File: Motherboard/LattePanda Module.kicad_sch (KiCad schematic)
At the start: 89 parts, among them IC78 PCM2704CDBR, J3 Conn_01x03_Pin, J5 SM03B-SRSS-TB, J78 Speaker_L, J79 Speaker_R, SW78 SW_Push, SW79 SW_Push, SW80 SW_Push, SW81 SW_Push, U10 ULC0524P, U11 ULC0524P, U12 ULC0524P, U78 RP2040, U84 PAM8403D, U88 RP2354B, U95 W25Q128JVS, Y1 ABM8-272-T3, Y2 ABM8-272-T3, Y78 Crystal

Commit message: Multiplexed Debug HDMI port with DDIB screen, there are no BIOS versions with HDMI out on TCP1.
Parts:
- added IC79: TS3DV621RUAR, QFN50P350X900X80-43N-D, symbol TS3DV621RUAR:TS3DV621RUAR
- added SW82: SW_Nidec_CAS-120A1, Button_Switch_SMD:Nidec_Copal_CAS-120A, symbol Switch:SW_Nidec_CAS-120A1
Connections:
- net +3V3: now also IC79.1 (VCC_1), IC79.17 (VCC_2), IC79.30 (VCC_3), IC79.8 (EN), SW82.3 (A)
- net DBUG_HPD: now also IC79.20 (HPDB); no longer A2.185 (TCP1_HPD)
- net DBUG_SCL: now also IC79.22 (AUX-B); no longer A2.175 (TCP1_DDC_SCL)
- net DBUG_SDA: now also IC79.24 (AUX+B); no longer A2.173 (TCP1_DDC_SDA)
- net DBUG_TX0+: now also IC79.42 (D0+B); no longer A2.220 (TCP1_TX0+)
- net DBUG_TX0-: now also IC79.40 (D0-B); no longer A2.222 (TCP1_TX0-)
- net DBUG_TX1+: now also IC79.37 (D1+B); no longer A2.226 (TCP1_TXRX0+)
- net DBUG_TX1-: now also IC79.35 (D1-B); no longer A2.228 (TCP1_TXRX0-)
- net DBUG_TX2+: now also IC79.33 (D2+B); no longer A2.232 (TCP1_TX1+)
- net DBUG_TX2-: now also IC79.31 (D2-B); no longer A2.234 (TCP1_TX1-)
- net DBUG_TX3+: now also IC79.28 (D3+B); no longer A2.238 (TCP1_TXRX1+)
- net DBUG_TX3-: now also IC79.26 (D3-B); no longer A2.240 (TCP1_TXRX1-)
- net DDIB_HPD: now also IC79.21 (HPDA); no longer A2.183 (DDIB_HPD)
- net DDIB_SCL: now also IC79.23 (AUX-A); no longer A2.171 (DDIB_DDC_SCL)
- net DDIB_SDA: now also IC79.25 (AUX+A); no longer A2.169 (DDIB_DDC_SDA)
- net DDIB_TX0+: now also IC79.41 (D0+A); no longer A2.217 (DDIB_TX0+)
- net DDIB_TX0-: now also IC79.39 (D0-A); no longer A2.215 (DDIB_TX0-)
- net DDIB_TX1+: now also IC79.38 (D1+A); no longer A2.211 (DDIB_TX1+)
- net DDIB_TX1-: now also IC79.36 (D1-A); no longer A2.209 (DDIB_TX1-)
- net DDIB_TX2+: now also IC79.34 (D2+A); no longer A2.205 (DDIB_TX2+)
- net DDIB_TX2-: now also IC79.32 (D2-A); no longer A2.203 (DDIB_TX2-)
- net DDIB_TX3+: now also IC79.29 (D3+A); no longer A2.199 (DDIB_TX3+)
- net DDIB_TX3-: now also IC79.27 (D3-A); no longer A2.197 (DDIB_TX3-)
- net GND: now also IC79.43 (EP_(GND)), SW82.1 (C)
- net SLS_S3: now also U88.42 (GPIO33)
- net ~{PWR_LED}/~{PSON}: now also U88.40 (GPIO32)
- new net: IC79.10 (SEL2), IC79.9 (SEL1), SW82.2 (B)
- new net DDI_HPD: A2.183 (DDIB_HPD), IC79.15 (HPD)
- new net DDI_SCL: A2.171 (DDIB_DDC_SCL), IC79.14 (AUX-)
- new net DDI_SDA: A2.169 (DDIB_DDC_SDA), IC79.13 (AUX+)
- new net DDI_TX0+: A2.217 (DDIB_TX0+), IC79.2 (D0+)
- new net DDI_TX0-: A2.215 (DDIB_TX0-), IC79.3 (D0-)
- new net DDI_TX1+: A2.211 (DDIB_TX1+), IC79.4 (D1+)
- new net DDI_TX1-: A2.209 (DDIB_TX1-), IC79.5 (D1-)
- new net DDI_TX2+: A2.205 (DDIB_TX2+), IC79.6 (D2+)
- new net DDI_TX2-: A2.203 (DDIB_TX2-), IC79.7 (D2-)
- new net DDI_TX3+: A2.199 (DDIB_TX3+), IC79.11 (D3+)
- new net DDI_TX3-: A2.197 (DDIB_TX3-), IC79.12 (D3-)
- no-connect marks 120 -> 131
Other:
- note removed: "(They are all used because I need an extra one to configure the ADV7611. Because we CANT have defaults, we MUST use I2C)"

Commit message: Quick Save
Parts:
- A2: LCSC Part C2761395 -> C962120; NOTE (none) -> LOTES ADDR0207-P001A connector
- H10, H9: LCSC Part C5301799 -> C2928178
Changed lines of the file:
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@@
 			)
 		)
-		(property "Sim.Device" ""
+		(property "NOTE" "LOTES ADDR0207-P001A connector"
 			(at 311.15 190.5 0)
 			(hide yes)
@@
 			)
 		)
-		(property "LCSC Part" "C2761395"
+		(property "LCSC Part" "C962120"
 			(at 311.15 190.5 0)
 			(hide yes)
@@
 			)
 		)
-		(property "Description" "SMTWEM250STR"
+		(property "Description" "SMTWE2025MTJ"
 			(at 297.18 345.44 0)
 			(hide yes)
@@
 			)
 		)
-		(property "LCSC Part" "C5301799"
+		(property "LCSC Part" "C2928178"
 			(at 297.18 345.44 0)
 			(hide yes)
@@
 			)
 		)
-		(property "Description" "SMTWEM250STR"
+		(property "Description" "SMTWE2025MTJ"
 			(at 322.58 345.44 0)
 			(hide yes)
@@
 			)
 		)
-		(property "LCSC Part" "C5301799"
+		(property "LCSC Part" "C2928178"
 			(at 322.58 345.44 0)
 			(hide yes)

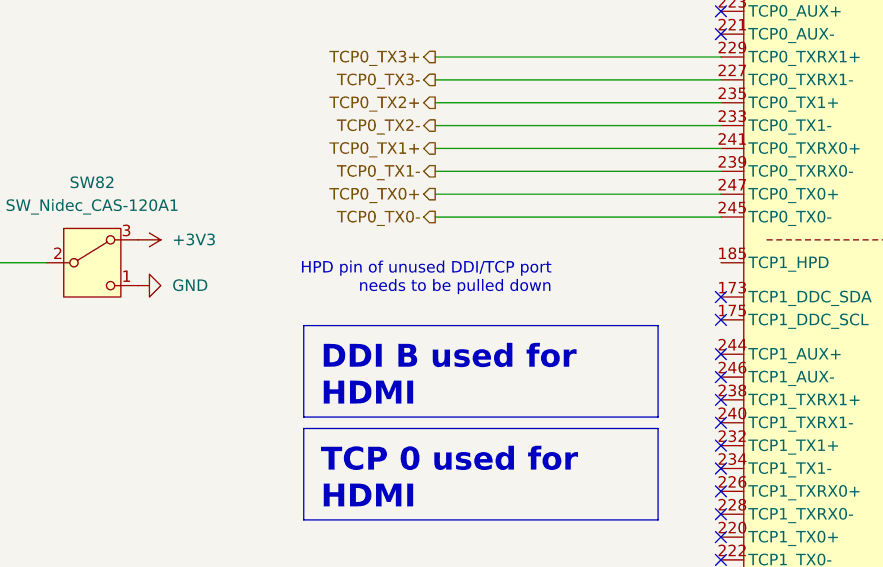
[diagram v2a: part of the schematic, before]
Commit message: Re-Routed DDIB Screen, pinout was previously flipped
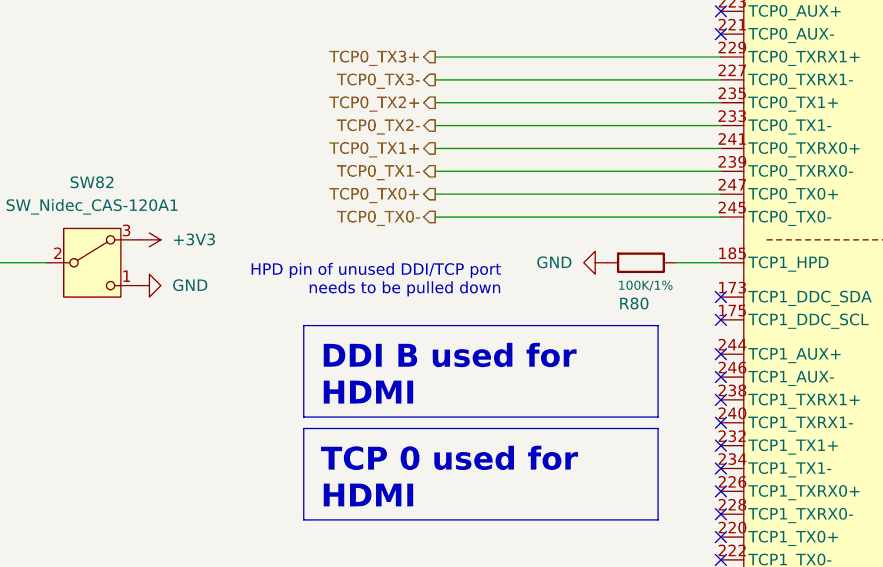
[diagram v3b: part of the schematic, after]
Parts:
- added R80: 100K/1%, A_HDJ_Library:R_0402_1005Metric, symbol Device:R
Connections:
- net GND: now also R80.2
- net at A2.185 (TCP1_HPD): now also R80.1

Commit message: Various fixes, and some peripheral routing
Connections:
- net Col3: no longer U88.79 (GPIO2)
- net Col4: no longer U88.80 (GPIO3)
- net RPi_HALL_L: now also U88.80 (GPIO3); no longer U88.20 (GPIO20)
- net RPi_LCD_EN: now also U88.79 (GPIO2); no longer U88.22 (GPIO22)
- net Row1: now also U88.2 (GPIO5); no longer U88.1 (GPIO4)
- net Row2: now also U88.3 (GPIO6); no longer U88.2 (GPIO5)
- net Row3: now also U88.1 (GPIO4); no longer U88.3 (GPIO6)
- no-connect marks 131 -> 132
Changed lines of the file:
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@@
 	)
 	(no_connect
+		(at 270.51 165.1)
+	)
+	(no_connect
 		(at 351.79 87.63)
 	)
@@
 		)
 	)
-	(hierarchical_label "Col3"
-		(shape output)
-		(at 510.54 130.81 0)
-		(effects
-			(font
-				(size 1.27 1.27)
-			)
-			(justify left)
-		)
-	)
 	(hierarchical_label "~{PWR_SW}"
 		(shape input)
@@
 		)
 	)
+	(hierarchical_label "Col4"
+		(shape output)
+		(at 541.02 133.35 0)
+		(effects
+			(font
+				(size 1.27 1.27)
+			)
+			(justify left)
+		)
+	)
 	(hierarchical_label "HSIO_3_TX+"
 		(shape output)
@@
 	(hierarchical_label "Row3"
 		(shape input)
-		(at 510.54 140.97 0)
+		(at 510.54 135.89 0)
 		(effects
 			(font
@@
 	(hierarchical_label "DDIB_TOUCH_SCL"
 		(shape input)
-		(at 351.79 220.98 0)
+		(at 351.79 220.98 180)
 		(effects
 			(font
 				(size 1.27 1.27)
 			)
-			(justify left)
+			(justify right)
 		)
 	)
 	(hierarchical_label "Row1"
 		(shape input)
-		(at 510.54 135.89 0)
+		(at 510.54 138.43 0)
 		(effects
 			(font
@@
 	(hierarchical_label "RPi_HALL_L"
 		(shape output)
-		(at 510.54 176.53 0)
+		(at 510.54 133.35 0)
 		(effects
 			(font
@@
 		)
 	)
-	(hierarchical_label "RPi_LCD_EN"
-		(shape passive)
-		(at 510.54 181.61 0)
-		(effects
-			(font
-				(size 1.27 1.27)
-			)
-			(justify left)
-		)
-	)
 	(hierarchical_label "TCP0_TX3-"
 		(shape output)
@@
 		)
 	)
+	(hierarchical_label "Col3"
+		(shape output)
+		(at 541.02 130.81 0)
+		(effects
+			(font
+				(size 1.27 1.27)
+			)
+			(justify left)
+		)
+	)
 	(hierarchical_label "TCP0_TX3+"
 		(shape output)
@@
 		)
 	)
-	(hierarchical_label "Col4"
-		(shape output)
-		(at 510.54 133.35 0)
-		(effects
-			(font
-				(size 1.27 1.27)
-			)
-			(justify left)
-		)
-	)
 	(hierarchical_label "DDIB_TOUCH_SDA"
 		(shape bidirectional)
@@
 		)
 	)
+	(hierarchical_label "RPi_LCD_EN"
+		(shape passive)
+		(at 510.54 130.81 0)
+		(effects
+			(font
+				(size 1.27 1.27)
+			)
+			(justify left)
+		)
+	)
 	(hierarchical_label "L_ADC_X"
 		(shape output)
@@
 	(hierarchical_label "TCP0_TOUCH_SCL"
 		(shape input)
-		(at 351.79 218.44 0)
+		(at 351.79 218.44 180)
 		(effects
 			(font
 				(size 1.27 1.27)
 			)
-			(justify left)
+			(justify right)
 		)
 	)
 	(hierarchical_label "Row2"
 		(shape input)
-		(at 510.54 138.43 0)
+		(at 510.54 140.97 0)
 		(effects
 			(font

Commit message: Updated CTRLs to be one sided (saves a billion dollars somehow), added LCSC_Parts for BOM, and other fixes. (Part 1/2)
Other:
- note added: "???"
- note added: "HSIO 2"
- note added: "HSIO 3"
- note added: "HSIO 6"
- note added: "HSIO 8"
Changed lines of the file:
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@@
+		)
+	)
+	(text "HSIO 3\n\n\n"
+		(exclude_from_sim no)
+		(at 335.026 101.092 0)
+		(effects
+			(font
+				(size 1.27 1.27)
+			)
 		)
 	)
@@
 		)
 	)
+	(text "HSIO 8\n\n"
+		(exclude_from_sim no)
+		(at 335.026 95.25 0)
+		(effects
+			(font
+				(size 1.27 1.27)
+			)
+		)
+	)
 	(text "Sleeping State Signal\n\n- SLS_S0: \n  - S0 (Working): HIGH\n  - S3 (Slpeeping): LOW\n  - S4 (Hibernation): LOW\n  - S5 (Soft Off): LOW\n- SLS_S3:\n  - S0 (Working): HIGH\n  - S3 (Slpeeping): HIGH\n  - S4 (Hibernation): LOW\n  - S5 (Soft Off): LOW"
 		(exclude_from_sim no)
@@
 		)
 	)
+	(text "HSIO 6\n\n\n\n"
+		(exclude_from_sim no)
+		(at 335.28 107.696 0)
+		(effects
+			(font
+				(size 1.27 1.27)
+			)
+		)
+	)
 	(text "USB2_P6 is reserved for TypeC PD Controller\nDO NOT use it as a normal USB"
 		(exclude_from_sim no)
@@
 			)
 			(justify left)
+		)
+	)
+	(text "???\n"
+		(exclude_from_sim no)
+		(at 336.804 89.154 0)
+		(effects
+			(font
+				(size 1.27 1.27)
+			)
 		)
 	)
@@
 		)
 	)
+	(text "HSIO 8\n\n\n\n"
+		(exclude_from_sim no)
+		(at 263.652 129.286 0)
+		(effects
+			(font
+				(size 1.27 1.27)
+			)
+		)
+	)
+	(text "HSIO 6\n\n\n\n"
+		(exclude_from_sim no)
+		(at 264.16 171.958 0)
+		(effects
+			(font
+				(size 1.27 1.27)
+			)
+		)
+	)
 	(text "Have to send just 1 message on this I2C lane,\nbecause 5A charging isn't the default, 1A is. \nThis makes charging take 5hrs instead of 25.\nWHY... I HATE I2C."
 		(exclude_from_sim no)
@@
 		)
 	)
+	(text "HSIO 2\n"
+		(exclude_from_sim no)
+		(at 335.026 84.074 0)
+		(effects
+			(font
+				(size 1.27 1.27)
+			)
+		)
+	)

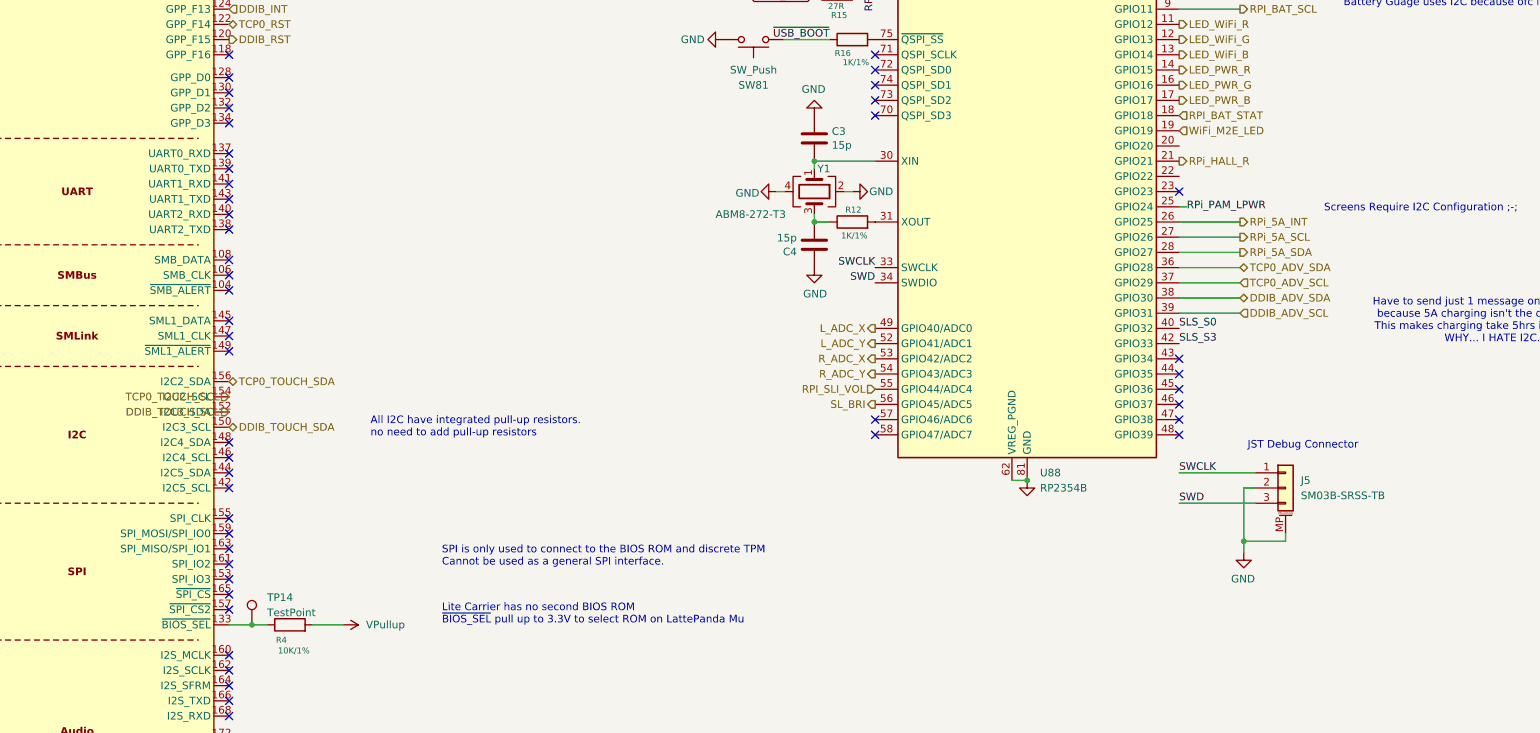
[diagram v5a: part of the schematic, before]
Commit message: Completed routing of 9V and 3.3V of PSU
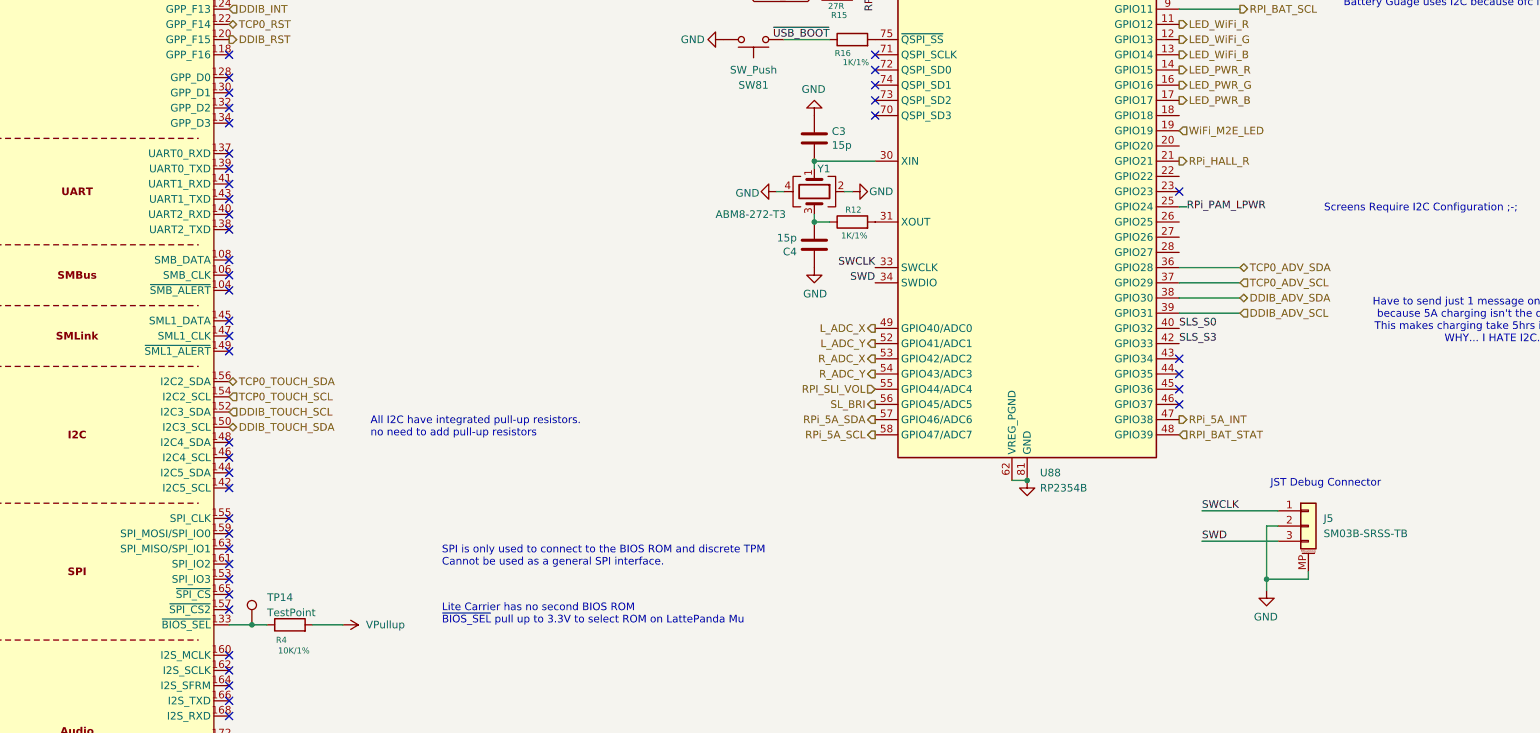
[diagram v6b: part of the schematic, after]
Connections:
- net RPI_BAT_STAT: now also U88.48 (GPIO39); no longer U88.18 (GPIO18)
- net RPi_5A_INT: now also U88.47 (GPIO38); no longer U88.26 (GPIO25)
- net RPi_5A_SCL: now also U88.58 (GPIO47/ADC7); no longer U88.27 (GPIO26)
- net RPi_5A_SDA: now also U88.57 (GPIO46/ADC6); no longer U88.28 (GPIO27)
- no-connect marks 132 -> 128
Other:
- moved on the sheet: J5
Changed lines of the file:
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@@
 	(text "JST Debug Connector"
 		(exclude_from_sim no)
-		(at 521.97 227.33 0)
+		(at 525.78 233.68 0)
 		(effects
 			(font
@@
 	)
 	(junction
-		(at 521.335 242.57)
+		(at 525.145 248.92)
 		(diameter 0)
 		(color 0 0 0 0)
@@
 	)
 	(no_connect
-		(at 459.74 222.25)
-	)
-	(no_connect
 		(at 270.51 299.72)
 	)
@@
 	)
 	(no_connect
-		(at 459.74 224.79)
-	)
-	(no_connect
 		(at 270.51 149.86)
 	)
@@
 	)
 	(no_connect
-		(at 510.54 224.79)
-	)
-	(no_connect
-		(at 510.54 222.25)
-	)
-	(no_connect
 		(at 270.51 157.48)
 	)
@@
 	(wire
 		(pts
-			(xy 521.335 233.68) (xy 521.335 242.57)
+			(xy 525.145 240.03) (xy 525.145 248.92)
 		)
 		(stroke
@@
 	(wire
 		(pts
-			(xy 510.54 231.14) (xy 523.24 231.14)
+			(xy 514.35 237.49) (xy 527.05 237.49)
 		)
 		(stroke
@@
 	(wire
 		(pts
-			(xy 528.32 241.3) (xy 528.32 242.57)
+			(xy 532.13 247.65) (xy 532.13 248.92)
 		)
 		(stroke
@@
 	(wire
 		(pts
-			(xy 510.54 236.22) (xy 523.24 236.22)
+			(xy 514.35 242.57) (xy 527.05 242.57)
 		)
 		(stroke
@@
 	(wire
 		(pts
-			(xy 520.7 189.23) (xy 510.54 189.23)
-		)
-		(stroke
-			(width 0)
-			(type default)
-		)
-	)
-	(wire
-		(pts
 			(xy 351.79 119.38) (xy 369.57 119.38)
 		)
@@
 	(wire
 		(pts
-			(xy 520.7 194.31) (xy 510.54 194.31)
-		)
-		(stroke
-			(width 0)
-			(type default)
-		)
-	)
-	(wire
-		(pts
 			(xy 459.74 328.93) (xy 459.74 334.01)
 		)
@@
 	(wire
 		(pts
-			(xy 521.335 242.57) (xy 528.32 242.57)
+			(xy 525.145 248.92) (xy 532.13 248.92)
 		)
 		(stroke
@@
 	(wire
 		(pts
-			(xy 521.335 242.57) (xy 521.335 244.475)
+			(xy 525.145 248.92) (xy 525.145 250.825)
 		)
 		(stroke
@@
 	(wire
 		(pts
-			(xy 520.7 191.77) (xy 510.54 191.77)
-		)
-		(stroke
-			(width 0)
-			(type default)
-		)
-	)
-	(wire
-		(pts
 			(xy 520.7 199.39) (xy 510.54 199.39)
 		)
@@
 	(wire
 		(pts
-			(xy 523.24 233.68) (xy 521.335 233.68)
+			(xy 527.05 240.03) (xy 525.145 240.03)
 		)
 		(stroke
@@
 	)
 	(label "SWD"
-		(at 510.54 236.22 0)
+		(at 514.35 242.57 0)
 		(effects
 			(font
@@
 	)
 	(label "SWCLK"
-		(at 510.54 231.14 0)
+		(at 514.35 237.49 0)
 		(effects
 			(font
@@
 		)
 	)
+	(hierarchical_label "RPi_5A_SCL"
+		(shape output)
+		(at 459.74 224.79 180)
+		(effects
+			(font
+				(size 1.27 1.27)
+			)
+			(justify right)
+		)
+	)
 	(hierarchical_label "LED_WiFi_B"
 		(shape output)
@@
 		)
 	)
-	(hierarchical_label "RPi_5A_SDA"
-		(shape output)
-		(at 520.7 194.31 0)
-		(effects
-			(font
-				(size 1.27 1.27)
-			)
-			(justify left)
-		)
-	)
 	(hierarchical_label "RPI_BAT_SDA"
 		(shape bidirectional)
@@
 		)
 	)
+	(hierarchical_label "RPi_5A_SDA"
+		(shape output)
+		(at 459.74 222.25 180)
+		(effects
+			(font
+				(size 1.27 1.27)
+			)
+			(justify right)
+		)
+	)
 	(hierarchical_label "DBUG_TX0-"
 		(shape output)
@@
 	(hierarchical_label "RPI_BAT_STAT"
 		(shape input)
-		(at 510.54 171.45 0)
+		(at 510.54 224.79 0)
 		(effects
 			(font
@@
 	(hierarchical_label "DDIB_TOUCH_SCL"
 		(shape input)
-		(at 351.79 220.98 180)
+		(at 351.79 220.98 0)
 		(effects
 			(font
 				(size 1.27 1.27)
 			)
-			(justify right)
+			(justify left)
 		)
 	)
@@
 		)
 	)
+	(hierarchical_label "RPi_5A_INT"
+		(shape output)
+		(at 510.54 222.25 0)
+		(effects
+			(font
+				(size 1.27 1.27)
+			)
+			(justify left)
+		)
+	)
 	(hierarchical_label "Col3"
 		(shape output)
@@
 		)
 	)
-	(hierarchical_label "RPi_5A_INT"
-		(shape output)
-		(at 520.7 189.23 0)
-		(effects
-			(font
-				(size 1.27 1.27)
-			)
-			(justify left)
-		)
-	)
 	(hierarchical_label "HSIO_2_TX-"
 		(shape output)
@@
 		)
 	)
-	(hierarchical_label "RPi_5A_SCL"
-		(shape output)
-		(at 520.7 191.77 0)
-		(effects
-			(font
-				(size 1.27 1.27)
-			)
-			(justify left)
-		)
-	)
 	(hierarchical_label "HSIO_3_RX-"
 		(shape input)
@@
 	(hierarchical_label "TCP0_TOUCH_SCL"
 		(shape input)
-		(at 351.79 218.44 180)
+		(at 351.79 218.44 0)
 		(effects
 			(font
 				(size 1.27 1.27)
 			)
-			(justify right)
+			(justify left)
 		)
 	)
@@
 	(symbol
 		(lib_id "power:GND")
-		(at 521.335 244.475 0)
+		(at 525.145 250.825 0)
 		(mirror y)
 		(unit 1)
@@
 		(dnp no)
 		(property "Reference" "#PWR038"
-			(at 521.335 250.825 0)
+			(at 525.145 257.175 0)
 			(hide yes)
 			(show_name no)
@@
 		)
 		(property "Value" "GND"
-			(at 521.208 248.8692 0)
+			(at 525.018 255.2192 0)
 			(show_name no)
 			(do_not_autoplace no)
@@
 		)
 		(property "Footprint" ""
-			(at 521.335 244.475 0)
+			(at 525.145 250.825 0)
 			(hide yes)
 			(show_name no)
@@
 		)
 		(property "Datasheet" ""
-			(at 521.335 244.475 0)
+			(at 525.145 250.825 0)
 			(hide yes)
 			(show_name no)
@@
 		)
 		(property "Description" ""
-			(at 521.335 244.475 0)
+			(at 525.145 250.825 0)
 			(show_name no)
 			(do_not_autoplace no)
@@
 	(symbol
 		(lib_id "Connector_Generic_MountingPin:Conn_01x03_MountingPin")
-		(at 528.32 233.68 0)
+		(at 532.13 240.03 0)
 		(unit 1)
 		(body_style 1)
@@
 		(fields_autoplaced yes)
 		(property "Reference" "J5"
-			(at 530.86 232.41 0)
+			(at 534.67 238.76 0)
 			(show_name no)
 			(do_not_autoplace no)
@@
 		)
 		(property "Value" "SM03B-SRSS-TB"
-			(at 530.86 234.95 0)
+			(at 534.67 241.3 0)
 			(show_name no)
 			(do_not_autoplace no)
@@
 		)
 		(property "Footprint" "Connector_JST:JST_SH_SM03B-SRSS-TB_1x03-1MP_P1.00mm_Horizontal"
-			(at 528.32 233.68 0)
+			(at 532.13 240.03 0)
 			(hide yes)
 			(show_name no)
@@
 		)
 		(property "Datasheet" ""
-			(at 528.32 233.68 0)
+			(at 532.13 240.03 0)
 			(hide yes)
 			(show_name no)
@@
 		)
 		(property "Description" ""
-			(at 528.32 233.68 0)
+			(at 532.13 240.03 0)
 			(show_name no)
 			(do_not_autoplace no)

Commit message: Finished Power Management system (5V done this commit)
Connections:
- net Row2: now also U88.4 (GPIO7); no longer U88.3 (GPIO6)
- net Row4: now also U88.3 (GPIO6); no longer U88.4 (GPIO7)
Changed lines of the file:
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@@
 	(hierarchical_label "Row4"
 		(shape input)
-		(at 510.54 143.51 0)
+		(at 510.54 140.97 0)
 		(effects
 			(font
@@
 	(hierarchical_label "Row2"
 		(shape input)
-		(at 510.54 140.97 0)
-		(effects
-			(font
+		(at 510.54 143.51 0)
+		(effects
+			(font
